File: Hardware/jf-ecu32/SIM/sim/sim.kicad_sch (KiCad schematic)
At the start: 10 parts, among them U2 ${SIM.PARAMS}

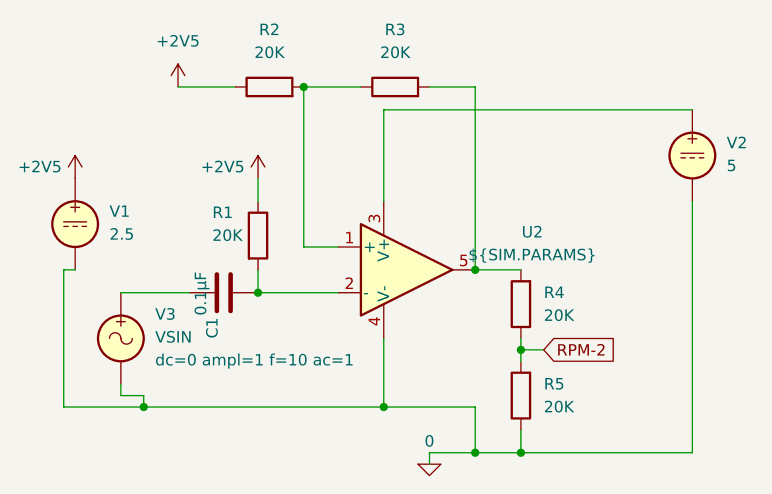
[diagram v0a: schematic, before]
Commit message: Log on SD or SPIFFS
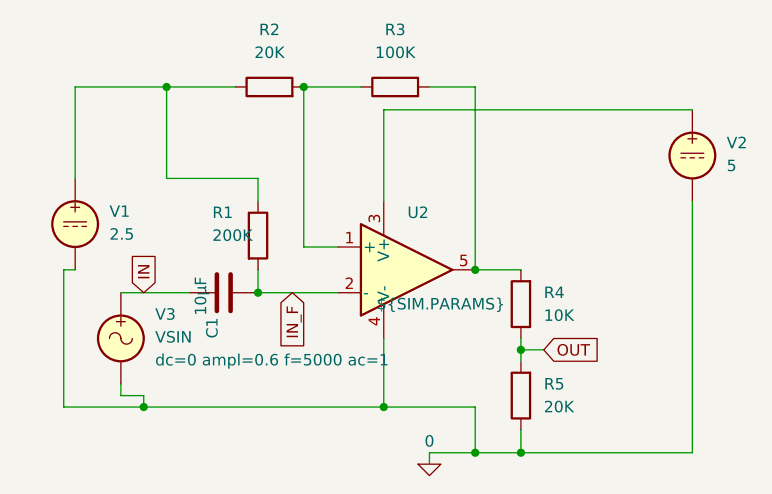
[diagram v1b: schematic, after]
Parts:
- C1: value 0.1µF -> 10µF
- R1: value 20K -> 200K
- R3: value 20K -> 100K
- R4: value 20K -> 10K
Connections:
- net IN: now reaches C1.1, V3.1
- net IN_F: now reaches C1.2, R1.2, U2.2 (-)
- net +2V5: no longer names the net of R1.1, R2.1, V1.1
- net RPM-2 renamed OUT
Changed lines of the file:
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@@
   (junction (at 38.1 69.85) (diameter 0) (color 0 0 0 0)
   )
+  (junction (at 40.64 34.29) (diameter 0) (color 0 0 0 0)
+  )
   (junction (at 64.77 69.85) (diameter 0) (color 0 0 0 0)
   )
@@
     (stroke (width 0) (type default))
   )
+  (wire (pts (xy 40.64 34.29) (xy 48.26 34.29))
+    (stroke (width 0) (type default))
+  )
   (wire (pts (xy 69.85 76.2) (xy 69.85 74.93))
     (stroke (width 0) (type default))
@@
     (stroke (width 0) (type default))
   )
+  (wire (pts (xy 30.48 34.29) (xy 30.48 44.45))
+    (stroke (width 0) (type default))
+  )
   (wire (pts (xy 29.21 54.61) (xy 30.48 54.61))
     (stroke (width 0) (type default))
   )
+  (wire (pts (xy 50.8 44.45) (xy 40.64 44.45))
+    (stroke (width 0) (type default))
+  )
+  (wire (pts (xy 40.64 44.45) (xy 40.64 34.29))
+    (stroke (width 0) (type default))
+  )
   (wire (pts (xy 69.85 34.29) (xy 74.93 34.29))
     (stroke (width 0) (type default))
@@
     (stroke (width 0) (type default))
   )
-  (wire (pts (xy 41.91 34.29) (xy 48.26 34.29))
+  (wire (pts (xy 30.48 34.29) (xy 40.64 34.29))
     (stroke (width 0) (type default))
   )
@@
     (stroke (width 0) (type default))
   )
-  (global_label "RPM-2" (shape input) (at 82.55 63.5 0) (fields_autoplaced)
+  (global_label "IN" (shape input) (at 38.1 57.15 90) (fields_autoplaced)
     (effects (font (size 1.27 1.27)) (justify left))
-    (property "Intersheetrefs" "${INTERSHEET_REFS}" (at 91.7364 63.4206 0)
+    (property "Intersheetrefs" "${INTERSHEET_REFS}" (at 38.1 52.2295 90)
+      (effects (font (size 1.27 1.27)) (justify left) hide)
+    )
+  )
+  (global_label "IN_F" (shape input) (at 54.61 57.15 270) (fields_autoplaced)
+    (effects (font (size 1.27 1.27)) (justify right))
+    (property "Intersheetrefs" "${INTERSHEET_REFS}" (at 54.61 64.1267 90)
+      (effects (font (size 1.27 1.27)) (justify right) hide)
+    )
+  )
+  (global_label "OUT" (shape input) (at 82.55 63.5 0) (fields_autoplaced)
+    (effects (font (size 1.27 1.27)) (justify left))
+    (property "Intersheetrefs" "${INTERSHEET_REFS}" (at 89.1638 63.5 0)
       (effects (font (size 1.27 1.27)) (justify left) hide)
     )
@@
       (effects (font (size 1.27 1.27)) hide)
     )
-    (property "Sim.Params" "dc=0 ampl=1 f=10 ac=1" (at 39.37 64.6402 0)
+    (property "Sim.Params" "dc=0 ampl=0.6 f=5000 ac=1" (at 39.37 64.6402 0)
       (effects (font (size 1.27 1.27)) (justify left))
     )
@@
       (effects (font (size 1.27 1.27)) (justify right))
     )
-    (property "Value" "20K" (at 82.55 59.6899 0)
+    (property "Value" "10K" (at 82.55 59.6899 0)
       (effects (font (size 1.27 1.27)) (justify right))
     )
@@
       (effects (font (size 1.27 1.27)) (justify left))
     )
-    (property "Value" "0.1µF" (at 44.45 59.69 0)
+    (property "Value" "10µF" (at 44.45 59.69 0)
       (effects (font (size 1.27 1.27)) (justify left))
     )
@@
       (effects (font (size 1.27 1.27)))
     )
-    (property "Value" "20K" (at 66.04 30.48 90)
+    (property "Value" "100K" (at 66.04 30.48 90)
       (effects (font (size 1.27 1.27)))
     )
@@
     )
   )
-  (symbol (lib_id "power:+2V5") (at 50.8 44.45 0) (unit 1)
+  (symbol (lib_id "Simulation_SPICE:OPAMP") (at 67.31 54.61 0) (unit 1)
     (in_bom yes) (on_board yes) (dnp no)
-    (property "Reference" "#PWR02" (at 50.8 48.26 0)
-      (effects (font (size 1.27 1.27)) hide)
-    )
-    (property "Value" "+2V5" (at 44.45 43.18 0)
-      (effects (font (size 1.27 1.27)) (justify left))
-    )
-    (property "Footprint" "" (at 50.8 44.45 0)
-      (effects (font (size 1.27 1.27)) hide)
-    )
-    (property "Datasheet" "" (at 50.8 44.45 0)
-      (effects (font (size 1.27 1.27)) hide)
-    )
-    (pin "1")
-    (instances
-      (project "sim"
-        (path "/02c48faa-c9f6-4a84-92e5-b93315c4bd5e"
-          (reference "#PWR02") (unit 1)
-        )
-      )
-    )
-  )
-  (symbol (lib_id "Simulation_SPICE:OPAMP") (at 67.31 54.61 0) (unit 1)
-    (in_bom yes) (on_board yes) (dnp no) (fields_autoplaced)
-    (property "Reference" "U2" (at 81.28 50.4191 0)
-      (effects (font (size 1.27 1.27)))
-    )
-    (property "Value" "${SIM.PARAMS}" (at 81.28 52.9591 0)
+    (property "Reference" "U2" (at 68.58 48.26 0)
+      (effects (font (size 1.27 1.27)))
+    )
+    (property "Value" "${SIM.PARAMS}" (at 71.12 58.42 0)
       (effects (font (size 1.27 1.27)))
     )
@@
     )
   )
-  (symbol (lib_id "power:+2V5") (at 30.48 44.45 0) (unit 1)
-    (in_bom yes) (on_board yes) (dnp no)
-    (property "Reference" "#PWR03" (at 30.48 48.26 0)
-      (effects (font (size 1.27 1.27)) hide)
-    )
-    (property "Value" "+2V5" (at 24.13 43.18 0)
-      (effects (font (size 1.27 1.27)) (justify left))
-    )
-    (property "Footprint" "" (at 30.48 44.45 0)
-      (effects (font (size 1.27 1.27)) hide)
-    )
-    (property "Datasheet" "" (at 30.48 44.45 0)
-      (effects (font (size 1.27 1.27)) hide)
-    )
-    (pin "1")
-    (instances
-      (project "sim"
-        (path "/02c48faa-c9f6-4a84-92e5-b93315c4bd5e"
-          (reference "#PWR03") (unit 1)
-        )
-      )
-    )
-  )
   (symbol (lib_id "Device:R") (at 50.8 50.8 0) (unit 1)
     (in_bom yes) (on_board yes) (dnp no)
@@
       (effects (font (size 1.27 1.27)) (justify left))
     )
-    (property "Value" "20K" (at 45.72 50.8 0)
+    (property "Value" "200K" (at 45.72 50.8 0)
       (effects (font (size 1.27 1.27)) (justify left))
     )
@@
         )
       )
-    )
-  )
-  (symbol (lib_id "power:+2V5") (at 41.91 34.29 0) (unit 1)
-    (in_bom yes) (on_board yes) (dnp no) (fields_autoplaced)
-    (property "Reference" "#PWR01" (at 41.91 38.1 0)
-      (effects (font (size 1.27 1.27)) hide)
-    )
-    (property "Value" "+2V5" (at 41.91 29.21 0)
-      (effects (font (size 1.27 1.27)))
-    )
-    (property "Footprint" "" (at 41.91 34.29 0)
-      (effects (font (size 1.27 1.27)) hide)
-    )
-    (property "Datasheet" "" (at 41.91 34.29 0)
-      (effects (font (size 1.27 1.27)) hide)
-    )
-    (pin "1")
-    (instances
-      (project "sim"
-        (path "/02c48faa-c9f6-4a84-92e5-b93315c4bd5e"
-          (reference "#PWR01") (unit 1)
-        )
-      )
